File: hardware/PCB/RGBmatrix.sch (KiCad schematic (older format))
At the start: 44 parts

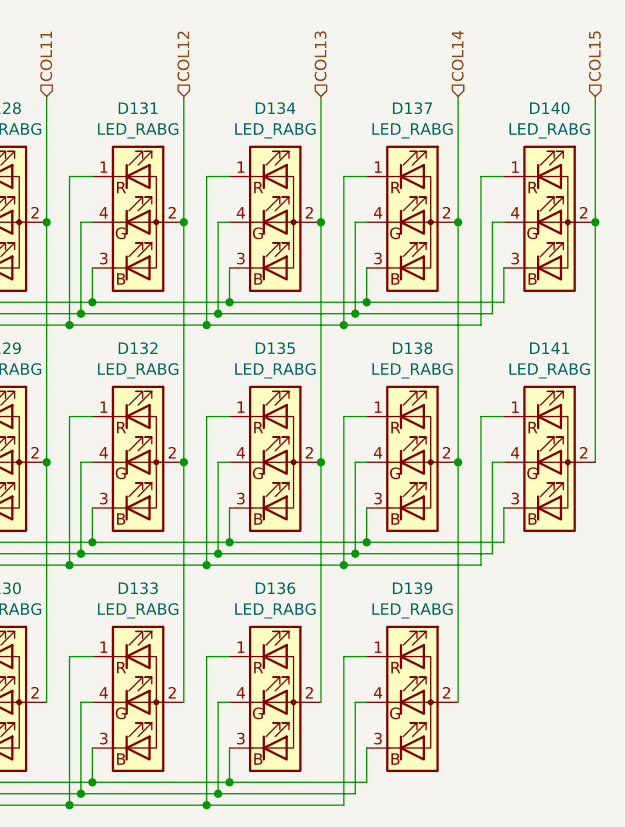
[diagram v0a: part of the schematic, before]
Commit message: Line up most parts and fix some problems with the part
1.Fix the LED footprint size
2.Edit the hotplug to be simpler (removed 2 holes)
3.Line up everything and the silkscreen
4. Fix the LED matrix and the switch matrix sch
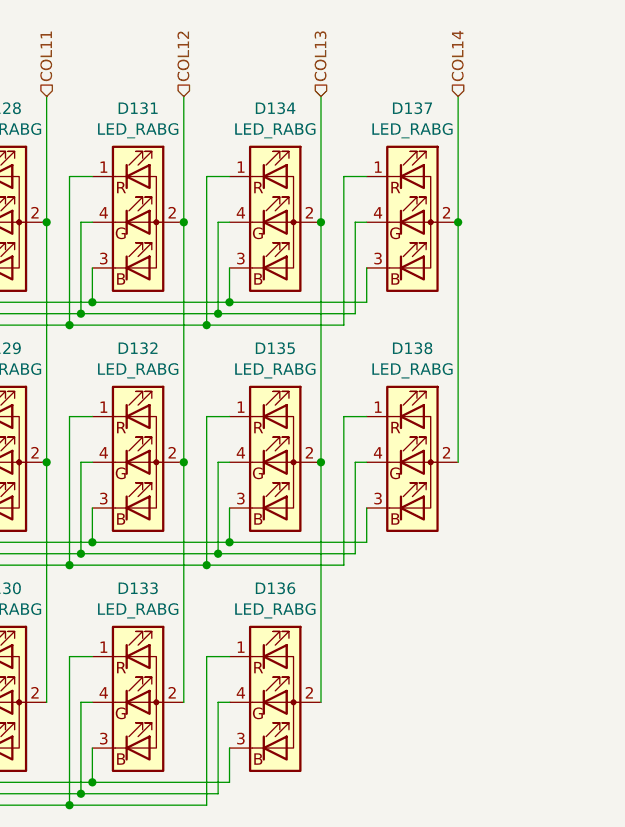
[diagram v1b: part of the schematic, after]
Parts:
- removed D139, D140, D141: LED_RABG, KiCad:XZMDKCBDDG45S9, symbol Device:LED_RABG
- D100, D101, D102, D103, D104, D105, D106, D107, D108, D109, D110, D111, D112, D113, D114, D115, D116, D117, D118, D119, D120, D121, D122, D123, D124, D125, D126, D127, D128, D129, D130, D131, D132, D133, D134, D135, D136, D137, D138, D98, D99: footprint KiCad:XZMDKCBDDG45S9 -> KiCad:XZMDKCBDDG45S9_fixed

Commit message: Making progress, so many distance warning!!!
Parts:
- renumbered D102 to D100, D103 to D101, D104 to D102, D105 to D103, D106 to D104, D107 to D105, D108 to D106, D109 to D107, D110 to D108, D111 to D109, D112 to D110, D113 to D111, D114 to D112, D115 to D113, D116 to D114, D117 to D115, D118 to D116, D119 to D117, D120 to D118, D121 to D119, D122 to D120, D123 to D121, D124 to D122, D125 to D123, D126 to D124, D127 to D125, D128 to D126, D129 to D127, D130 to D128, D131 to D129, D132 to D130, D133 to D131, D134 to D132, D135 to D133, D136 to D134, D137 to D135, D138 to D136, D98 to D96, D99 to D97, D100 to D98, D101 to D99

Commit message: alot of changes
modify the QFN-48 so PCB 3d view in future would look better (so I don't design a part that doesn't fit)
I made a useless QFN-40 3d model
modify schematics so it looks better
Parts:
- D100, D101, D102, D103, D104, D105, D106, D107, D108, D109, D110, D111, D112, D113, D114, D115, D116, D117, D118, D119, D120, D121, D122, D123, D124, D125, D126, D127, D128, D129, D130, D131, D132, D133, D134, D135, D136, D96, D97, D98, D99: Footprint (none) -> KiCad:XZMDKCBDDG45S9_fixed; Value (none) -> XZMDKCBDDG45S9

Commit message: making progress
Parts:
- D100, D101, D102, D103, D104, D105, D106, D107, D108, D109, D110, D111, D112, D113, D114, D115, D116, D117, D118, D119, D120, D121, D122, D123, D124, D125, D126, D127, D128, D129, D130, D131, D132, D133, D134, D135, D136, D96, D97, D98, D99: value LED_RABG -> XZMDKCBDDG45S-9

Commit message: Now it should be working just fine
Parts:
- D100, D101, D102, D103, D104, D105, D106, D107, D108, D109, D110, D111, D112, D113, D114, D115, D116, D117, D118, D119, D120, D121, D122, D123, D124, D125, D126, D127, D128, D129, D130, D131, D132, D133, D134, D135, D136, D96, D97, D98, D99: Footprint KiCad:XZMDKCBDDG45S9_fixed -> (none); Value XZMDKCBDDG45S9 -> (none)

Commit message: add in part number so I could use it for the bom
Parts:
- D100, D101, D102, D103, D104, D105, D106, D107, D108, D109, D110, D111, D112, D113, D114, D115, D116, D117, D118, D119, D120, D121, D122, D123, D124, D125, D126, D127, D128, D129, D130, D131, D132, D133, D134, D135, D136, D96, D97, D98, D99: Part Number (none) -> XZMDKCBDDG45S-9
